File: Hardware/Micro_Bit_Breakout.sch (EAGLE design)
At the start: 9 parts, among them J1 EDGE-80PTH-RA, J2 M22PTH

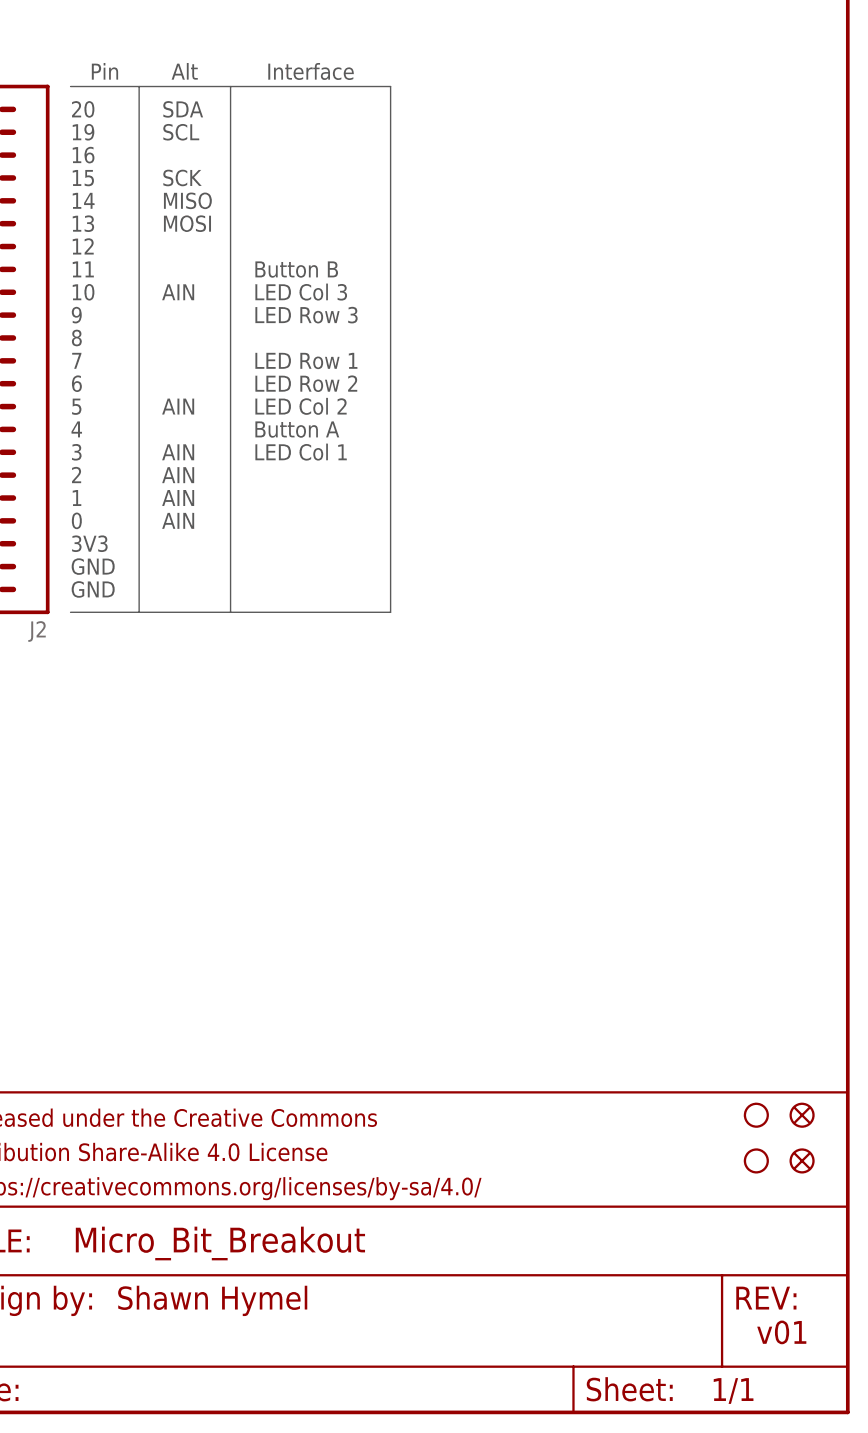
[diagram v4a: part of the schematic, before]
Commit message: Changed pins to match new micro:bit pinout. Updated to v10. Ready for review.
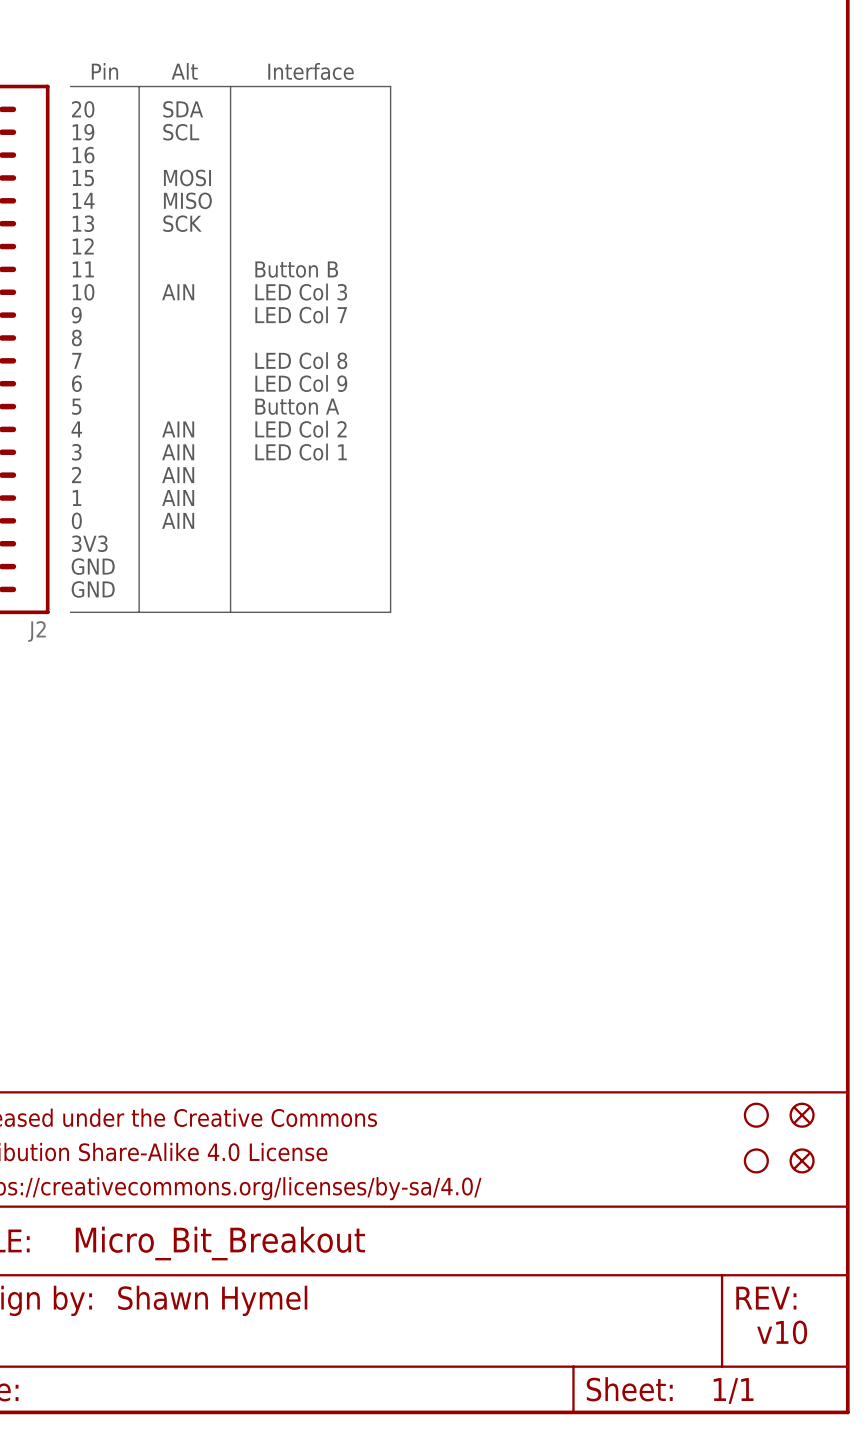
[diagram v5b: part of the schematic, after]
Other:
- note added: "LED Col 7"
- note added: "LED Col 8"
- note added: "LED Col 9"
- note added: "v10"
- note removed: "LED Row 1"
- note removed: "LED Row 2"
- note removed: "LED Row 3"
- note removed: "v01"
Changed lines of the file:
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@@
 <setting verticaltext="up"/>
 </settings>
-<grid distance="0.1" unitdist="inch" unit="inch" style="lines" multiple="1" display="yes" altdistance="0.01" altunitdist="inch" altunit="inch"/>
+<grid distance="0.1" unitdist="inch" unit="inch" style="lines" multiple="1" display="no" altdistance="0.01" altunitdist="inch" altunit="inch"/>
 <layers>
 <layer number="1" name="Top" color="4" fill="1" visible="no" active="no"/>
@@
 <plain>
 <text x="167.64" y="12.7" size="2.54" layer="94" align="center-left">Shawn Hymel</text>
-<text x="238.76" y="7.62" size="2.54" layer="94">v01</text>
+<text x="238.76" y="7.62" size="2.54" layer="94">v10</text>
 <text x="162.56" y="93.98" size="1.778" layer="97" rot="R180" align="center-right">GND</text>
 <text x="162.56" y="91.44" size="1.778" layer="97" rot="R180" align="center-right">GND</text>
@@
 <text x="172.72" y="142.24" size="1.778" layer="97" rot="R180" align="center-right">SCL</text>
 <text x="172.72" y="144.78" size="1.778" layer="97" rot="R180" align="center-right">SDA</text>
-<text x="172.72" y="132.08" size="1.778" layer="97" rot="R180" align="center-right">MOSI</text>
+<text x="172.72" y="132.08" size="1.778" layer="97" rot="R180" align="center-right">SCK</text>
 <text x="172.72" y="134.62" size="1.778" layer="97" rot="R180" align="center-right">MISO</text>
-<text x="172.72" y="137.16" size="1.778" layer="97" rot="R180" align="center-right">SCK</text>
+<text x="172.72" y="137.16" size="1.778" layer="97" rot="R180" align="center-right">MOSI</text>
 <text x="172.72" y="104.14" size="1.778" layer="97" rot="R180" align="center-right">AIN</text>
 <text x="172.72" y="99.06" size="1.778" layer="97" rot="R180" align="center-right">AIN</text>
 <text x="172.72" y="101.6" size="1.778" layer="97" rot="R180" align="center-right">AIN</text>
 <text x="172.72" y="106.68" size="1.778" layer="97" rot="R180" align="center-right">AIN</text>
-<text x="172.72" y="111.76" size="1.778" layer="97" rot="R180" align="center-right">AIN</text>
+<text x="172.72" y="109.22" size="1.778" layer="97" rot="R180" align="center-right">AIN</text>
 <text x="172.72" y="124.46" size="1.778" layer="97" rot="R180" align="center-right">AIN</text>
 <text x="182.88" y="127" size="1.778" layer="97" rot="R180" align="center-right">Button B</text>
 <text x="182.88" y="124.46" size="1.778" layer="97" rot="R180" align="center-right">LED Col 3</text>
-<text x="182.88" y="121.92" size="1.778" layer="97" rot="R180" align="center-right">LED Row 3</text>
-<text x="182.88" y="116.84" size="1.778" layer="97" rot="R180" align="center-right">LED Row 1</text>
-<text x="182.88" y="114.3" size="1.778" layer="97" rot="R180" align="center-right">LED Row 2</text>
-<text x="182.88" y="111.76" size="1.778" layer="97" rot="R180" align="center-right">LED Col 2</text>
-<text x="182.88" y="109.22" size="1.778" layer="97" rot="R180" align="center-right">Button A</text>
+<text x="182.88" y="121.92" size="1.778" layer="97" rot="R180" align="center-right">LED Col 7</text>
+<text x="182.88" y="116.84" size="1.778" layer="97" rot="R180" align="center-right">LED Col 8</text>
+<text x="182.88" y="114.3" size="1.778" layer="97" rot="R180" align="center-right">LED Col 9</text>
+<text x="182.88" y="109.22" size="1.778" layer="97" rot="R180" align="center-right">LED Col 2</text>
+<text x="182.88" y="111.76" size="1.778" layer="97" rot="R180" align="center-right">Button A</text>
 <text x="182.88" y="106.68" size="1.778" layer="97" rot="R180" align="center-right">LED Col 1</text>
 <wire x1="198.12" y1="147.32" x2="198.12" y2="88.9" width="0.1524" layer="97"/>

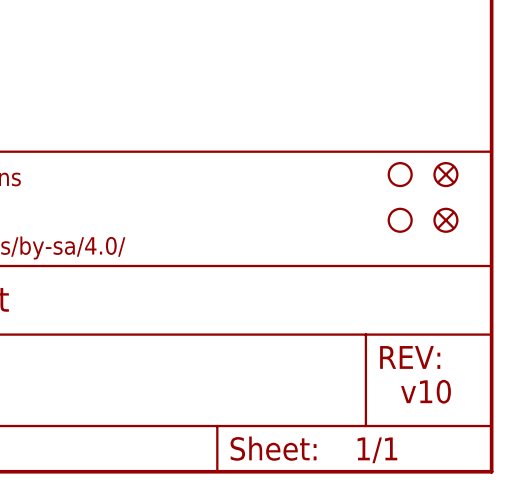
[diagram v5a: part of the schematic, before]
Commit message: Moved top up 0.1 inches. Added bottom fiducials. Added dimensions note for measurements.
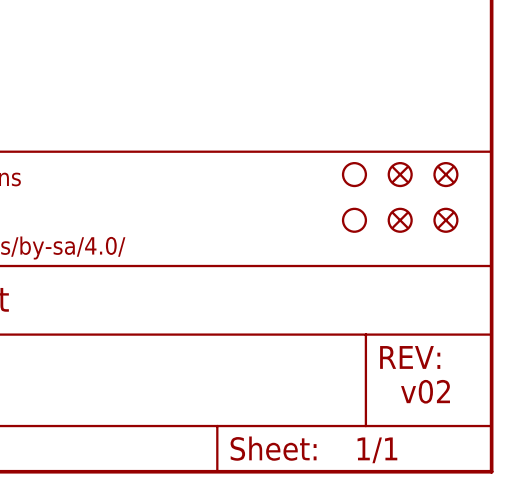
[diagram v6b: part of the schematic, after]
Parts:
- added FD3, FD4: FIDUCIAL1X2, SparkFun-Aesthetics:FIDUCIAL1X2
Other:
- note added: "v02"
- note removed: "v10"
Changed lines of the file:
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@@
 <setting verticaltext="up"/>
 </settings>
-<grid distance="0.1" unitdist="inch" unit="inch" style="lines" multiple="1" display="no" altdistance="0.01" altunitdist="inch" altunit="inch"/>
+<grid distance="0.1" unitdist="inch" unit="inch" style="lines" multiple="1" display="yes" altdistance="0.01" altunitdist="inch" altunit="inch"/>
 <layers>
 <layer number="1" name="Top" color="4" fill="1" visible="no" active="no"/>
@@
 <part name="SUPPLY1" library="SparkFun-Aesthetics" deviceset="3.3V" device=""/>
 <part name="SUPPLY2" library="SparkFun-Aesthetics" deviceset="3.3V" device=""/>
+<part name="FD3" library="SparkFun-Aesthetics" deviceset="FIDUCIAL" device="1X2"/>
+<part name="FD4" library="SparkFun-Aesthetics" deviceset="FIDUCIAL" device="1X2"/>
 </parts>
 <sheets>
@@
 <plain>
 <text x="167.64" y="12.7" size="2.54" layer="94" align="center-left">Shawn Hymel</text>
-<text x="238.76" y="7.62" size="2.54" layer="94">v10</text>
+<text x="238.76" y="7.62" size="2.54" layer="94">v02</text>
 <text x="162.56" y="93.98" size="1.778" layer="97" rot="R180" align="center-right">GND</text>
 <text x="162.56" y="91.44" size="1.778" layer="97" rot="R180" align="center-right">GND</text>
@@
 <instance part="FD1" gate="G$1" x="243.84" y="33.02"/>
 <instance part="FD2" gate="G$1" x="243.84" y="27.94"/>
-<instance part="H1" gate="G$1" x="238.76" y="33.02"/>
-<instance part="H2" gate="G$1" x="238.76" y="27.94"/>
+<instance part="H1" gate="G$1" x="233.68" y="33.02"/>
+<instance part="H2" gate="G$1" x="233.68" y="27.94"/>
 <instance part="LOGO3" gate="G$1" x="73.66" y="10.16"/>
 <instance part="GND2" gate="1" x="68.58" y="53.34"/>
@@
 <instance part="SUPPLY1" gate="G$1" x="127" y="104.14"/>
 <instance part="SUPPLY2" gate="G$1" x="139.7" y="101.6"/>
+<instance part="FD3" gate="G$1" x="238.76" y="33.02"/>
+<instance part="FD4" gate="G$1" x="238.76" y="27.94"/>
 </instances>
 <busses>

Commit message: v03
-Replaced micro:bit connector with SMD version
-Replaced silk with buzzard labels
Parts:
- removed J1: EDGE-80PTH-RA, local_lib:EDGE-80PTH-RA
- added U1: micro:bit, SparkFun-Connectors:MICRO:BIT_RA
- J2: value M22PTH -> CONN_22_NOSILK; device local_lib:M22PTH -> SparkFun-Connectors:CONN_22_NOSILK
- LOGO3: value OSHW-LOGOS -> OSHW-LOGOM; device SparkFun-Aesthetics:OSHW-LOGOS -> SparkFun-Aesthetics:OSHW-LOGOM
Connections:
- net 0: now also U1.P0; no longer J1.A36, J1.A37, J1.A38, J1.A39
- net 1: now also U1.P1; no longer J1.A28, J1.A29, J1.A30, J1.A31
- net 10: now also U1.P10; no longer J1.A25
- net 11: now also U1.P11; no longer J1.A24
- net 12: now also U1.P12; no longer J1.A23
- net 13: now also U1.P13; no longer J1.A18
- net 14: now also U1.P14; no longer J1.A17
- net 15: now also U1.P15; no longer J1.A16
- net 16: now also U1.P16; no longer J1.A15
- net 19: now also U1.P19; no longer J1.A8
- net 2: now also U1.P2; no longer J1.A19, J1.A20, J1.A21, J1.A22
- net 20: now also U1.P20; no longer J1.A7
- net 3: now also U1.P3; no longer J1.A40
- net 3.3V: now also U1.3.3V; no longer J1.A10, J1.A11, J1.A12, J1.A13, J1.A14, J1.A9
- net 4: now also U1.P4; no longer J1.A35
- net 5: now also U1.P5; no longer J1.A34
- net 6: now also U1.P6; no longer J1.A33
- net 7: now also U1.P7; no longer J1.A32
- net 8: now also U1.P8; no longer J1.A27
- net 9: now also U1.P9; no longer J1.A26
- net GND: now also U1.GND; no longer J1.A1, J1.A2, J1.A3, J1.A4, J1.A5, J1.A6
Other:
- note added: "Revised by: Alex Wende"
- note added: "v03"
- note removed: "v02"
